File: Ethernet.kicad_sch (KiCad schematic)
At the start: 31 parts, among them J7 RJ45_Hanrun_HR911105A_Horizon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, U5 LAN8720A, Y1 25MHz

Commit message: Finished route
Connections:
- net GND: now also Y1.2, Y1.4
- net RX_P: now reaches J7.3 (RD+), R13.2, U5.23 (RXP)
- net TX_N: now reaches J7.2 (TD-), R12.2, U5.20 (TXN)
- net TX_P: now reaches J7.1 (TD+), R11.2, U5.21 (TXP)
- net RX_N: now reaches J7.6 (RD-), R14.2, U5.22 (RXN)
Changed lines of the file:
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@@
+	)
+	(junction
+		(at 78.74 124.46)
+		(diameter 0)
+		(color 0 0 0 0)
 	)
 	(junction
@@
 	(wire
 		(pts
+			(xy 81.28 104.14) (xy 85.09 104.14)
+		)
+		(stroke
+			(width 0)
+			(type default)
+		)
+	)
+	(wire
+		(pts
 			(xy 78.74 124.46) (xy 78.74 120.65)
 		)
@@
 	(wire
 		(pts
+			(xy 72.39 104.14) (xy 72.39 124.46)
+		)
+		(stroke
+			(width 0)
+			(type default)
+		)
+	)
+	(wire
+		(pts
 			(xy 114.3 48.26) (xy 114.3 44.45)
 		)
@@
 	(wire
 		(pts
+			(xy 85.09 124.46) (xy 78.74 124.46)
+		)
+		(stroke
+			(width 0)
+			(type default)
+		)
+	)
+	(wire
+		(pts
 			(xy 111.76 34.29) (xy 111.76 50.8)
 		)
@@
 	(wire
 		(pts
+			(xy 85.09 104.14) (xy 85.09 124.46)
+		)
+		(stroke
+			(width 0)
+			(type default)
+		)
+	)
+	(wire
+		(pts
 			(xy 78.74 107.95) (xy 78.74 113.03)
 		)
@@
 		(pts
 			(xy 114.3 34.29) (xy 111.76 34.29)
+		)
+		(stroke
+			(width 0)
+			(type default)
+		)
+	)
+	(wire
+		(pts
+			(xy 76.2 104.14) (xy 72.39 104.14)
 		)
 		(stroke
@@
 		)
 	)
+	(label "RX_P"
+		(at 179.07 73.66 0)
+		(effects
+			(font
+				(size 1.27 1.27)
+			)
+			(justify left bottom)
+		)
+	)
+	(label "RX_N"
+		(at 179.07 78.74 0)
+		(effects
+			(font
+				(size 1.27 1.27)
+			)
+			(justify left bottom)
+		)
+	)
+	(label "TX_N"
+		(at 179.07 71.12 0)
+		(effects
+			(font
+				(size 1.27 1.27)
+			)
+			(justify left bottom)
+		)
+	)
+	(label "TX_P"
+		(at 179.07 66.04 0)
+		(effects
+			(font
+				(size 1.27 1.27)
+			)
+			(justify left bottom)
+		)
+	)

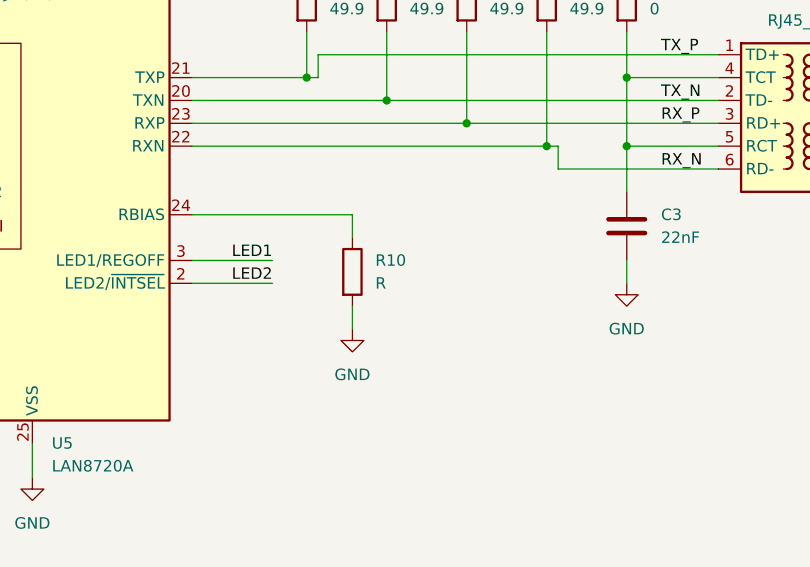
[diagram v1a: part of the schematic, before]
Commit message: Added lcsc power numbers
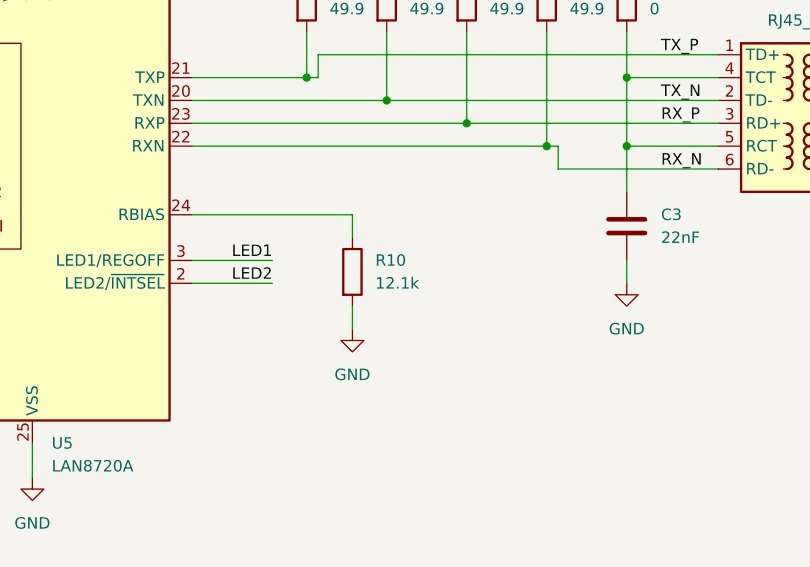
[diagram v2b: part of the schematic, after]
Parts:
- C10: LCSC (none) -> C1620
- C11: LCSC (none) -> C28323
- C12, C6, C9: LCSC (none) -> C1779
- C13, C14: LCSC (none) -> C1658
- C3: LCSC (none) -> C21122
- C4, C5, C7, C8: LCSC (none) -> C14663
- FB1: LCSC (none) -> C1002
- R10: value R -> 12.1k
- R15: LCSC (none) -> C21189
- R16, R19, R20, R21, R22, R23, R24: LCSC (none) -> C25804
- R17, R18: LCSC (none) -> C22966
- U5: LCSC (none) -> C45223
- Y1: LCSC (none) -> C9006
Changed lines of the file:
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@@
+			)
+		)
+		(property "LCSC" "C1658"
+			(at 67.31 116.84 0)
+			(effects
+				(font
+					(size 1.27 1.27)
+				)
+				(hide yes)
 			)
 		)
@@
 		)
 		(property "Description" "Unpolarized capacitor"
+			(at 129.54 40.64 0)
+			(effects
+				(font
+					(size 1.27 1.27)
+				)
+				(hide yes)
+			)
+		)
+		(property "LCSC" "C1779"
 			(at 129.54 40.64 0)
 			(effects
@@
 			)
 		)
+		(property "LCSC" "C25804"
+			(at 73.66 58.42 0)
+			(effects
+				(font
+					(size 1.27 1.27)
+				)
+				(hide yes)
+			)
+		)
 		(pin "1"
 		)
@@
 			)
 		)
+		(property "LCSC" "C1779"
+			(at 54.61 40.64 0)
+			(effects
+				(font
+					(size 1.27 1.27)
+				)
+				(hide yes)
+			)
+		)
 		(pin "1"
 		)
@@
 		)
 		(property "Description" "Unpolarized capacitor"
+			(at 69.85 40.64 0)
+			(effects
+				(font
+					(size 1.27 1.27)
+				)
+				(hide yes)
+			)
+		)
+		(property "LCSC" "C14663"
 			(at 69.85 40.64 0)
 			(effects
@@
 			)
 		)
-		(property "Value" "R"
+		(property "Value" "12.1k"
 			(at 147.32 91.4399 0)
 			(effects
@@
 			)
 		)
+		(property "LCSC" "C1779"
+			(at 96.52 40.64 0)
+			(effects
+				(font
+					(size 1.27 1.27)
+				)
+				(hide yes)
+			)
+		)
 		(pin "1"
 		)
@@
 			)
 		)
+		(property "LCSC" "C9006"
+			(at 78.74 104.14 90)
+			(effects
+				(font
+					(size 1.27 1.27)
+				)
+				(hide yes)
+			)
+		)
 		(pin "3"
 		)
@@
 			)
 		)
+		(property "LCSC" "C25804"
+			(at 237.49 76.2 90)
+			(effects
+				(font
+					(size 1.27 1.27)
+				)
+				(hide yes)
+			)
+		)
 		(pin "1"
 		)
@@
 			)
 		)
+		(property "LCSC" "C21189"
+			(at 175.26 59.69 0)
+			(effects
+				(font
+					(size 1.27 1.27)
+				)
+				(hide yes)
+			)
+		)
 		(pin "2"
 		)
@@
 			)
 		)
+		(property "LCSC" "C25804"
+			(at 58.42 116.84 0)
+			(effects
+				(font
+					(size 1.27 1.27)
+				)
+				(hide yes)
+			)
+		)
 		(pin "1"
 		)
@@
 		)
 		(property "Description" "Unpolarized capacitor"
+			(at 121.92 40.64 0)
+			(effects
+				(font
+					(size 1.27 1.27)
+				)
+				(hide yes)
+			)
+		)
+		(property "LCSC" "C14663"
 			(at 121.92 40.64 0)
 			(effects
@@
 			)
 		)
+		(property "LCSC" "C14663"
+			(at 114.3 40.64 0)
+			(effects
+				(font
+					(size 1.27 1.27)
+				)
+				(hide yes)
+			)
+		)
 		(pin "1"
 		)
@@
 			)
 		)
+		(property "LCSC" "C25804"
+			(at 50.8 96.52 0)
+			(effects
+				(font
+					(size 1.27 1.27)
+				)
+				(hide yes)
+			)
+		)
 		(pin "1"
 		)
@@
 			)
 		)
+		(property "LCSC" "C25804"
+			(at 81.28 58.42 0)
+			(effects
+				(font
+					(size 1.27 1.27)
+				)
+				(hide yes)
+			)
+		)
 		(pin "1"
 		)
@@
 			)
 		)
+		(property "LCSC" "C21122"
+			(at 175.26 85.09 0)
+			(effects
+				(font
+					(size 1.27 1.27)
+				)
+				(hide yes)
+			)
+		)
 		(pin "2"
 		)
@@
 			)
 		)
+		(property "LCSC" "C22966"
+			(at 237.49 78.74 90)
+			(effects
+				(font
+					(size 1.27 1.27)
+				)
+				(hide yes)
+			)
+		)
 		(pin "1"
 		)
@@
 			)
 		)
+		(property "LCSC" "C22966"
+			(at 237.49 68.58 90)
+			(effects
+				(font
+					(size 1.27 1.27)
+				)
+				(hide yes)
+			)
+		)
 		(pin "1"
 		)
@@
 			)
 		)
+		(property "LCSC" "C28323"
+			(at 88.9 40.64 0)
+			(effects
+				(font
+					(size 1.27 1.27)
+				)
+				(hide yes)
+			)
+		)
 		(pin "1"
 		)
@@
 			)
 		)
+		(property "LCSC" "C1002"
+			(at 109.22 29.21 90)
+			(effects
+				(font
+					(size 1.27 1.27)
+				)
+				(hide yes)
+			)
+		)
 		(pin "1"
 		)
@@
 			)
 		)
+		(property "LCSC" "C1620"
+			(at 81.28 40.64 0)
+			(effects
+				(font
+					(size 1.27 1.27)
+				)
+				(hide yes)
+			)
+		)
 		(pin "1"
 		)
@@
 		)
 		(property "Description" "Unpolarized capacitor"
+			(at 62.23 40.64 0)
+			(effects
+				(font
+					(size 1.27 1.27)
+				)
+				(hide yes)
+			)
+		)
+		(property "LCSC" "C14663"
 			(at 62.23 40.64 0)
 			(effects
@@
 			)
 		)
+		(property "LCSC" "C1658"
+			(at 78.74 116.84 0)
+			(effects
+				(font
+					(size 1.27 1.27)
+				)
+				(hide yes)
+			)
+		)
 		(pin "1"
 		)
@@
 			)
 		)
+		(property "LCSC" "C45223"
+			(at 109.22 81.28 0)
+			(effects
+				(font
+					(size 1.27 1.27)
+				)
+				(hide yes)
+			)
+		)
 		(pin "18"
 		)
@@
 			)
 		)
+		(property "LCSC" "C25804"
+			(at 66.04 58.42 0)
+			(effects
+				(font
+					(size 1.27 1.27)
+				)
+				(hide yes)
+			)
+		)
 		(pin "1"
 		)
@@
 			(at 58.42 58.42 0)
 			(effects
+				(font
+					(size 1.27 1.27)
+				)
+				(hide yes)
+			)
+		)
+		(property "LCSC" "C25804"
+			(at 58.42 58.42 0)
+			(effects
